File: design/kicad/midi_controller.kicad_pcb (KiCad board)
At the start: 4 copper layers, 166 x 166 mm, 26 parts, among them J1 Conn_01x02_Socket, J2 Conn_01x02_Socket, J3 Conn_01x02_Socket, J4 Conn_01x02_Socket, J5 Conn_01x02_Socket, J6 Conn_01x02_Socket, J7 Conn_01x05, SW1 MIDI_Switch_Pushbutton_PV0H24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, SW2 MIDI_Switch_Pushbutton_PV0H24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, SW3 MIDI_Switch_Pushbutton_PV0H24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

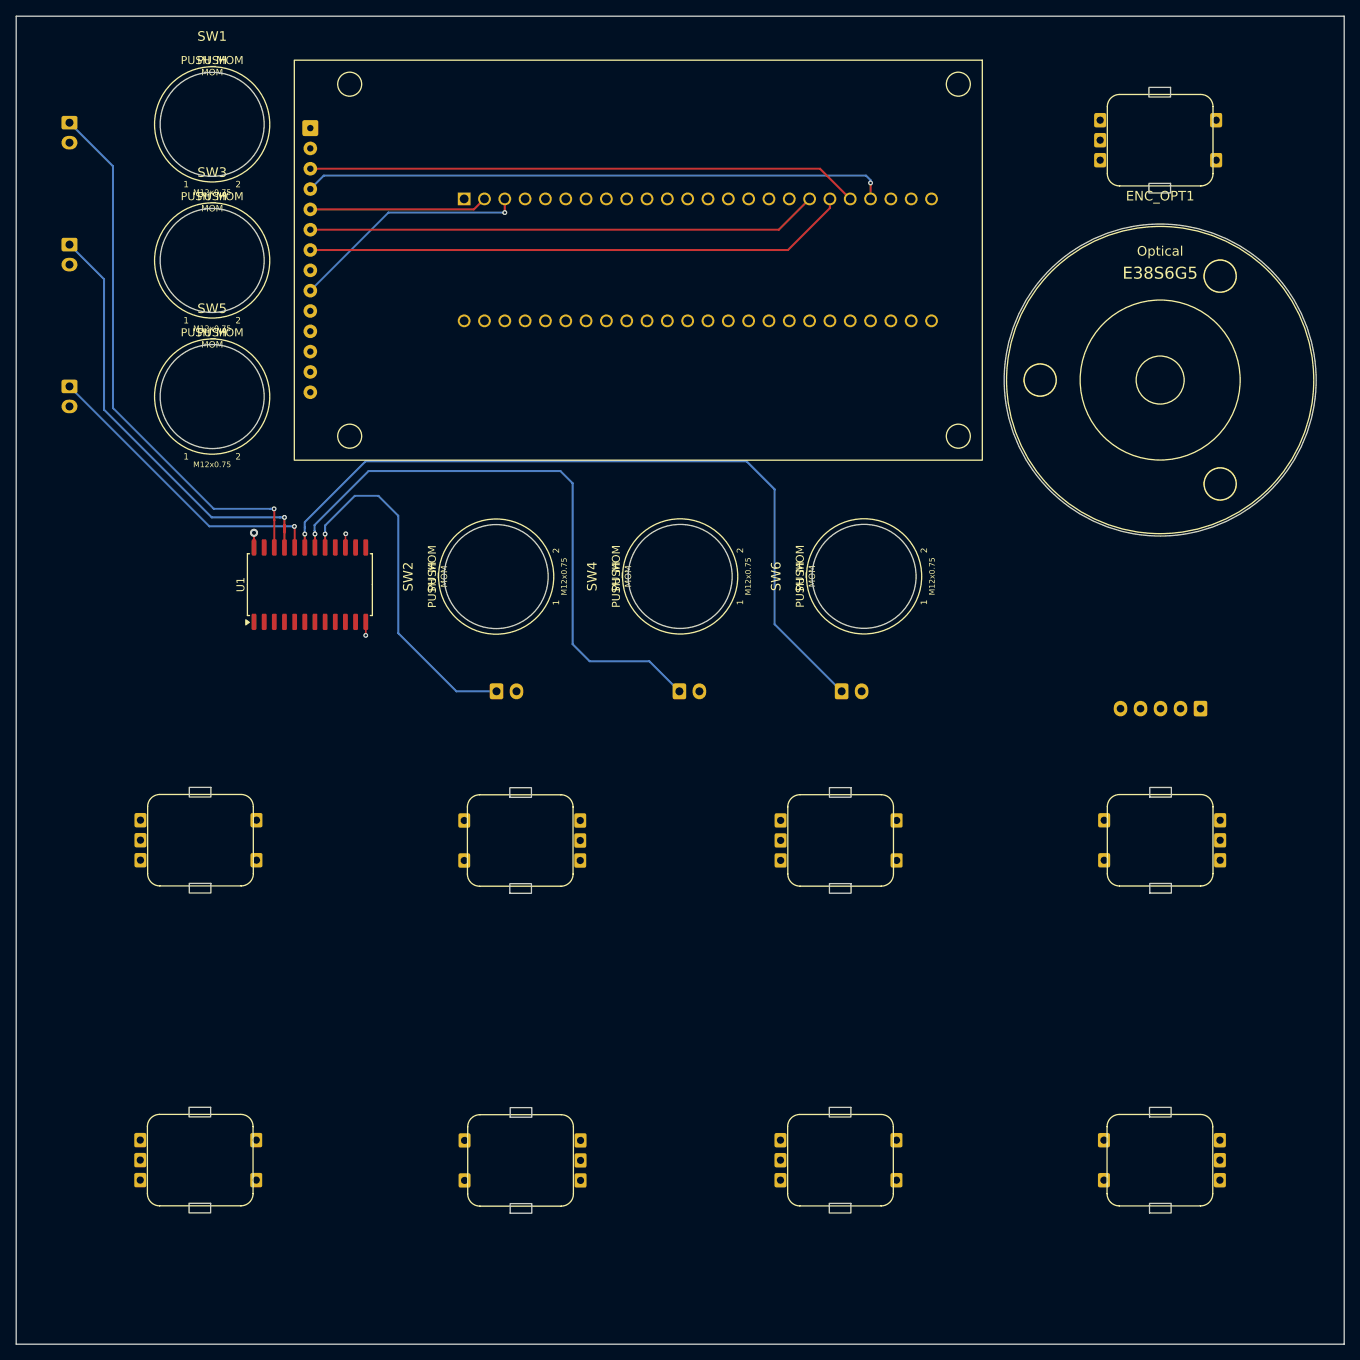
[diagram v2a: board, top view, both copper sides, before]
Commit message: Refactor MIDI controller design files
- Cleaned up hidden nets and net classes in the PCB layout file to improve clarity and maintainability.
- Adjusted visible layers to enhance the design view.
- Updated column widths in the properties section for better alignment.
- Modified schematic file by removing unnecessary wire elements and adding new ones for improved layout.
- Adjusted positions of various components and pins to ensure proper alignment and functionality.
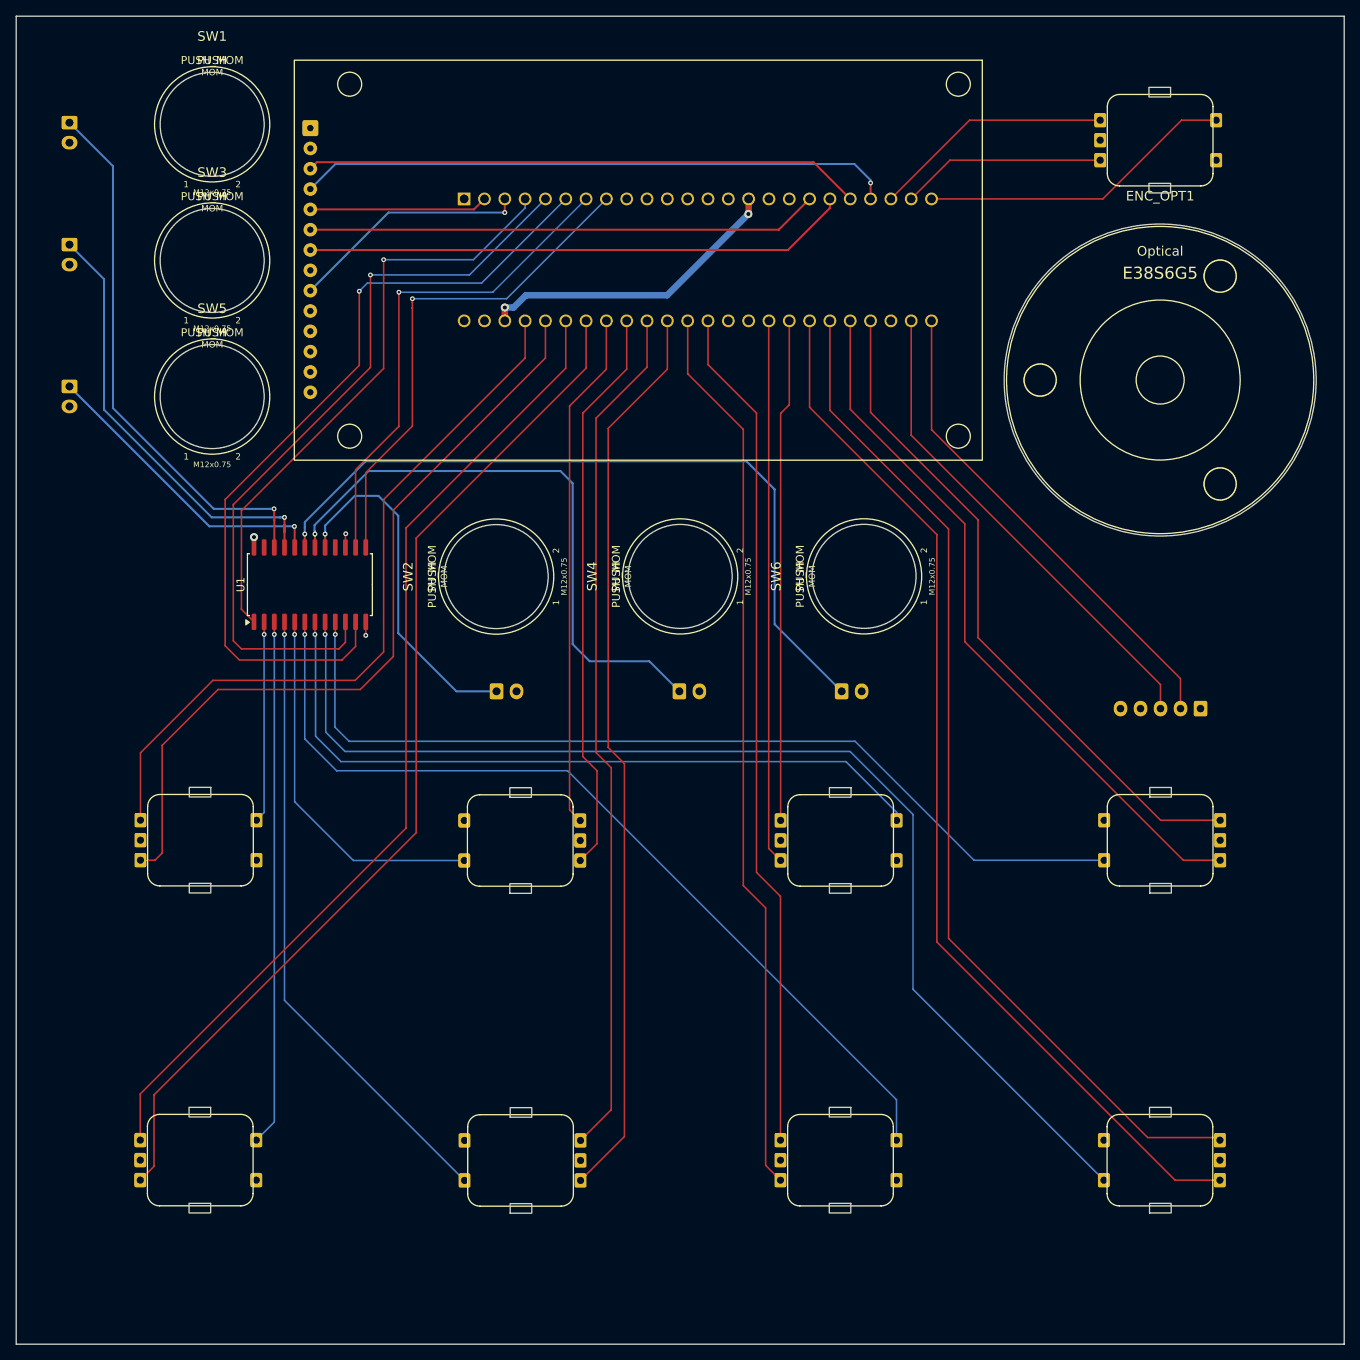
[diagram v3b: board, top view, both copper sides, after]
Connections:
- U1 pad 2: /MIDI_Encoder_Matrix_2x4_with_push_buttons/2x4_SW_A -> /MIDI_Encoder_Matrix_2x4_with_push_buttons/1x1_SW_A
- U1 pad 3: /MIDI_Encoder_Matrix_2x4_with_push_buttons/2x3_SW_A -> /MIDI_Encoder_Matrix_2x4_with_push_buttons/2x1_SW_A
- U1 pad 5: /MIDI_Encoder_Matrix_2x4_with_push_buttons/2x1_SW_A -> /MIDI_Encoder_Matrix_2x4_with_push_buttons/1x2_SW_A
- U1 pad 6: /MIDI_Encoder_Matrix_2x4_with_push_buttons/1x4_SW_A -> /MIDI_Encoder_Matrix_2x4_with_push_buttons/2x3_SW_A
- U1 pad 8: /MIDI_Encoder_Matrix_2x4_with_push_buttons/1x2_SW_A -> /MIDI_Encoder_Matrix_2x4_with_push_buttons/2x4_SW_A
- U1 pad 9: /MIDI_Encoder_Matrix_2x4_with_push_buttons/1x1_SW_A -> /MIDI_Encoder_Matrix_2x4_with_push_buttons/1x4_SW_A
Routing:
- net /MIDI_Encoder_Matrix_2x4_with_push_buttons/2x4_SW_A: track 0.00 -> 147.2 mm, vias 0 -> 1
- net /MIDI_Encoder_Matrix_2x4_with_push_buttons/2x4.QUAD_A: track 0.00 -> 131.9 mm
- net /MIDI_Encoder_Matrix_2x4_with_push_buttons/2x1.QUAD_B: track 0.00 -> 130.5 mm
- net /MIDI_Encoder_Matrix_2x4_with_push_buttons/2x4.QUAD_B: track 0.00 -> 127.7 mm
- net /MIDI_Encoder_Matrix_2x4_with_push_buttons/2x1.QUAD_A: track 0.00 -> 124.4 mm
- net /MIDI_Encoder_Matrix_2x4_with_push_buttons/1x4_SW_A: track 0.00 -> 116.3 mm, vias 0 -> 1
- net /MIDI_Encoder_Matrix_2x4_with_push_buttons/2x2.QUAD_A: track 0.00 -> 113.6 mm
- net /MIDI_Encoder_Matrix_2x4_with_push_buttons/2x3_SW_A: track 0.00 -> 112.4 mm, vias 0 -> 1
- net /MIDI_Encoder_Matrix_2x4_with_push_buttons/2x3.QUAD_B: track 0.00 -> 112.2 mm
- net /MIDI_Encoder_Matrix_2x4_with_push_buttons/2x2.QUAD_B: track 0.00 -> 107.5 mm
- net /MIDI_Encoder_Matrix_2x4_with_push_buttons/2x3.QUAD_A: track 0.00 -> 106.2 mm
- net S1: track 0.00 -> 102.7 mm, vias 0 -> 1
- net /MIDI_Encoder_Matrix_2x4_with_push_buttons/1x1.QUAD_B: track 0.00 -> 99.9 mm
- net S0: track 0.00 -> 96.0 mm, vias 0 -> 1
- net /MIDI_Encoder_Matrix_2x4_with_push_buttons/1x1.QUAD_A: track 0.00 -> 92.7 mm
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
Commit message: Refactor code structure for improved readability and maintainability
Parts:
- added C1: 100n, Capacitor_SMD:C_0805_2012Metric, F.Cu at (116.1, 92.4)
- added C2: 100n, Capacitor_SMD:C_0805_2012Metric, F.Cu at (168.6, 96.9)
- added C3: 100n, Capacitor_SMD:C_0805_2012Metric, F.Cu at (134.4, 117.7)
- added C4: 100n, Capacitor_SMD:C_0805_2012Metric, F.Cu at (106.8, 139.8)
- SW1, SW2, SW3, SW4, SW5, SW6: value MIDI_Switch_Pushbutton_PV0H24011 -> ~
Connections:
- net COM renamed /COM
- net ENC_A_OPT renamed /ENC_A_OPT
- net ENC_B_OPT renamed /ENC_B_OPT
- net S0 renamed /S0
- net S1 renamed /S1
- net S2 renamed /S2
- net S3 renamed /S3
- MCU1 pad 34: unconnected-(MCU1-GND-Pad34) -> GND
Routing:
- net GND: track 3.42 -> 13.5 mm, vias 2 -> 4
- net +5V: track 159.7 -> 167.3 mm, vias 0 -> 1
- net +3V3: track 114.2 -> 110.1 mm
- net Net-(D1-RST): track 74.5 -> 76.0 mm
- net Net-(D1-CS): track 69.7 -> 70.9 mm
- net /Buttons_Momentary/BUTTON_PUSH_MOM_02: track 55.2 -> 54.3 mm
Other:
- outline, holes or cut-outs redrawn
